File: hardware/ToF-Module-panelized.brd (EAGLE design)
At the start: 96.2 x 95.6 mm, 400 parts, among them CON1 JST-03, CON10 JST-03, CON11 JST-03, CON12 JST-03, CON13 JST-03, CON14 JST-03, CON15 JST-03, CON16 JST-03, CON17 JST-03, CON18 JST-03, CON19 JST-03, CON2 JST-03, CON20 JST-03, CON21 JST-03, CON22 JST-03, CON23 JST-03, CON24 JST-03, CON25 JST-03, CON26 JST-03, CON27 JST-03, CON28 JST-03, CON29 JST-03, CON3 JST-03, CON30 JST-03, CON31 JST-03, CON32 JST-03, CON33 JST-03, CON34 JST-03, CON35 JST-03, CON36 JST-03, CON37 JST-03, CON38 JST-03, CON39 JST-03, CON4 JST-03, CON40 JST-03, CON5 JST-03, CON6 JST-03, CON7 JST-03, CON8 JST-03, CON9 JST-03, U1 ATMEGA328P, U10 ATMEGA328P, U11 BSS138DWQ, U12 MIC5504_2.8YM5, U13 ATMEGA328P, U14 BSS138DWQ, U15 MIC5504_2.8YM5, U16 ATMEGA328P, U17 BSS138DWQ, U18 MIC5504_2.8YM5, U19 ATMEGA328P, U2 BSS138DWQ, U20 BSS138DWQ, U21 MIC5504_2.8YM5, U22 ATMEGA328P, U23 BSS138DWQ, U24 MIC5504_2.8YM5, U25 ATMEGA328P, U26 BSS138DWQ, U27 MIC5504_2.8YM5, U28 ATMEGA328P, U29 BSS138DWQ, U3 MIC5504_2.8YM5, U30 MIC5504_2.8YM5, U31 ATMEGA328P, U32 BSS138DWQ, U33 MIC5504_2.8YM5, U34 ATMEGA328P, U35 BSS138DWQ, U36 MIC5504_2.8YM5, U37 ATMEGA328P, U38 BSS138DWQ, U39 MIC5504_2.8YM5, U4 ATMEGA328P, U40 ATMEGA328P, U41 BSS138DWQ, U42 MIC5504_2.8YM5, U43 ATMEGA328P, U44 BSS138DWQ, U45 MIC5504_2.8YM5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

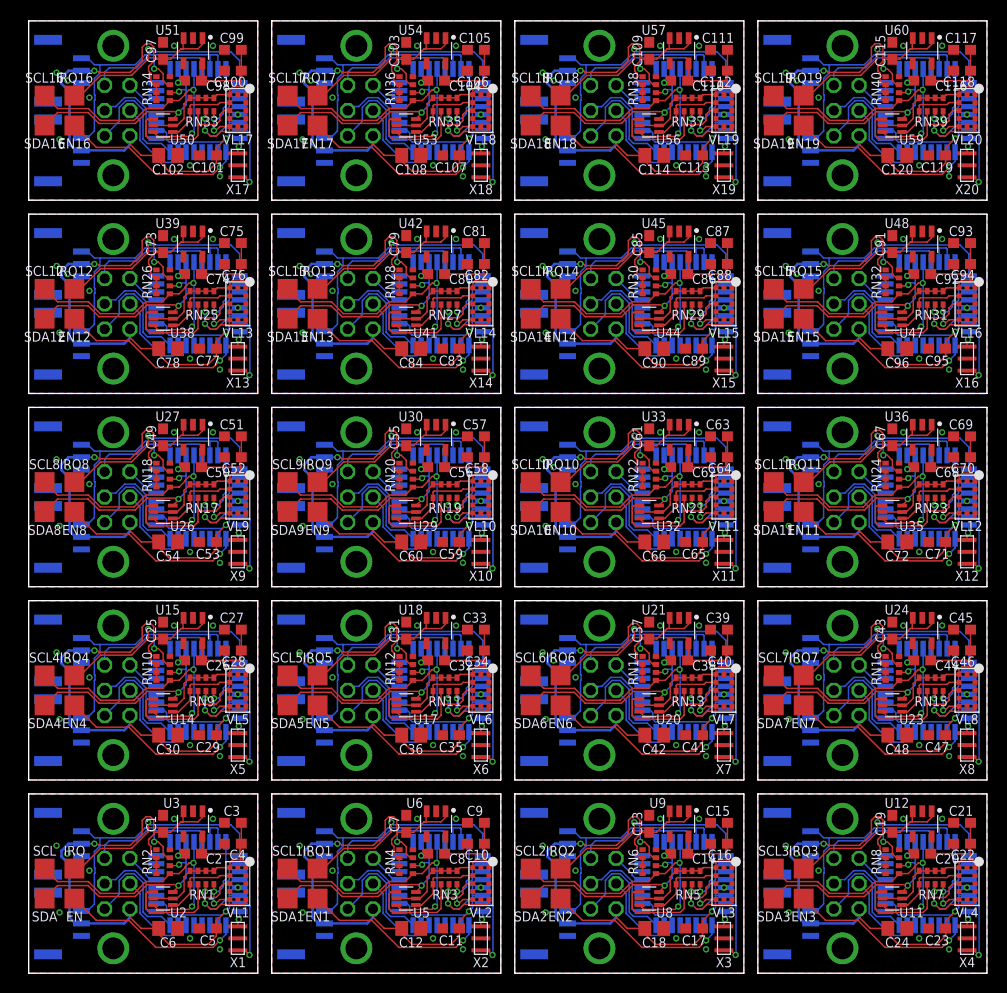
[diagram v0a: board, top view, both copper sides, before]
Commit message: hardware: add pullup for ext IRQ line + debug pads
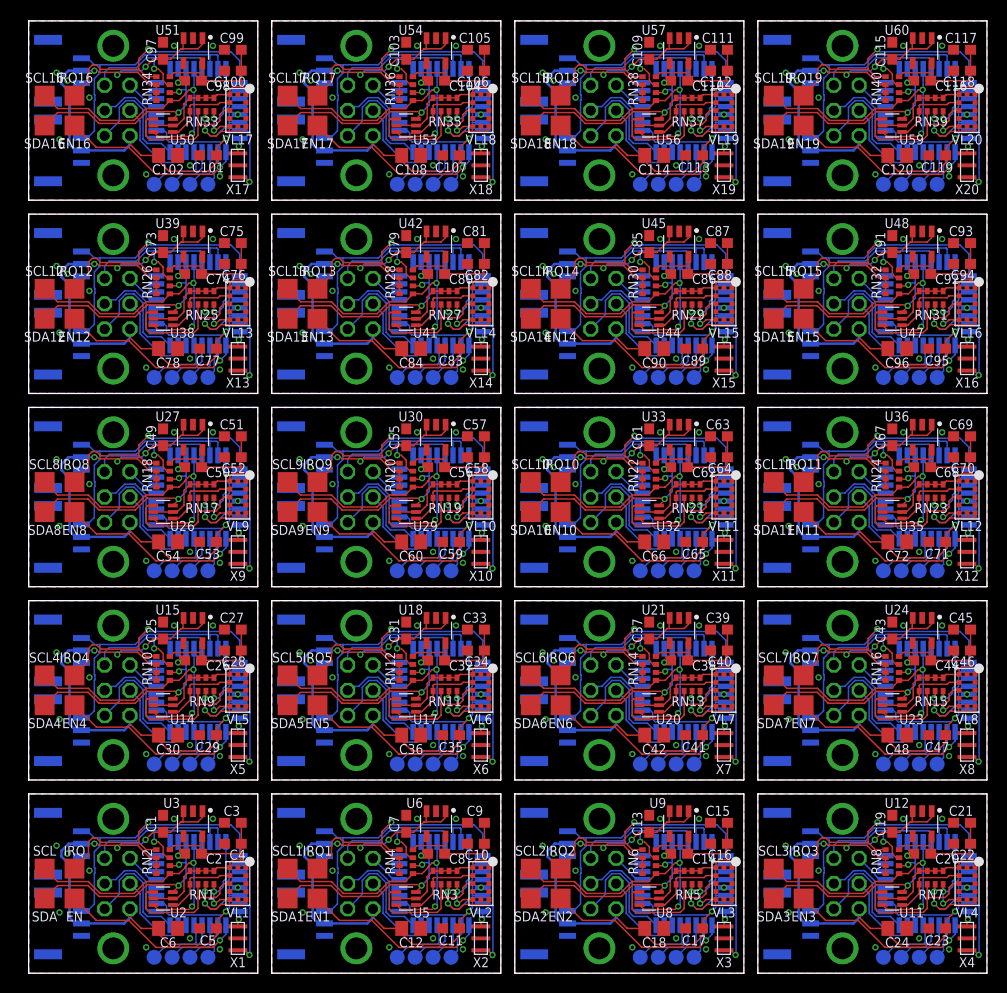
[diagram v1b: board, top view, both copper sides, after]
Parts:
- added DEBUG_A, DEBUG_A1, DEBUG_A10, DEBUG_A11, DEBUG_A12, DEBUG_A13, DEBUG_A14, DEBUG_A15, DEBUG_A16, DEBUG_A17, DEBUG_A18, DEBUG_A19, DEBUG_A2, DEBUG_A3, DEBUG_A4, DEBUG_A5, DEBUG_A6, DEBUG_A7, DEBUG_A8, DEBUG_A9, DEBUG_B, DEBUG_B1, DEBUG_B10, DEBUG_B11, DEBUG_B12, DEBUG_B13, DEBUG_B14, DEBUG_B15, DEBUG_B16, DEBUG_B17, DEBUG_B18, DEBUG_B19, DEBUG_B2, DEBUG_B3, DEBUG_B4, DEBUG_B5, DEBUG_B6, DEBUG_B7, DEBUG_B8, DEBUG_B9, DEBUG_C, DEBUG_C1, DEBUG_C10, DEBUG_C11, DEBUG_C12, DEBUG_C13, DEBUG_C14, DEBUG_C15, DEBUG_C16, DEBUG_C17, DEBUG_C18, DEBUG_C19, DEBUG_C2, DEBUG_C3, DEBUG_C4, DEBUG_C5, DEBUG_C6, DEBUG_C7, DEBUG_C8, DEBUG_C9, DEBUG_D, DEBUG_D1, DEBUG_D10, DEBUG_D11, DEBUG_D12, DEBUG_D13, DEBUG_D14, DEBUG_D15, DEBUG_D16, DEBUG_D17, DEBUG_D18, DEBUG_D19, DEBUG_D2, DEBUG_D3, DEBUG_D4, DEBUG_D5, DEBUG_D6, DEBUG_D7, DEBUG_D8, DEBUG_D9: PTR1TP15R, testpad:TP15R
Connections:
- new net N$1: DEBUG_A.TP, U1.10
- new net N$101: DEBUG_A12.TP, U37.10
- new net N$102: DEBUG_B12.TP, U37.11
- new net N$103: DEBUG_C12.TP, U37.12
- new net N$104: DEBUG_D12.TP, U37.13
- new net N$109: DEBUG_A13.TP, U40.10
- new net N$110: DEBUG_B13.TP, U40.11
- new net N$111: DEBUG_C13.TP, U40.12
- new net N$112: DEBUG_D13.TP, U40.13
- new net N$117: DEBUG_A14.TP, U43.10
- new net N$118: DEBUG_B14.TP, U43.11
- new net N$119: DEBUG_C14.TP, U43.12
- new net N$120: DEBUG_D14.TP, U43.13
- new net N$125: DEBUG_A15.TP, U46.10
- new net N$126: DEBUG_B15.TP, U46.11
- new net N$127: DEBUG_C15.TP, U46.12
- new net N$128: DEBUG_D15.TP, U46.13
- new net N$13: DEBUG_A1.TP, U4.10
- new net N$133: DEBUG_A16.TP, U49.10
- new net N$134: DEBUG_B16.TP, U49.11
- new net N$135: DEBUG_C16.TP, U49.12
- new net N$136: DEBUG_D16.TP, U49.13
- new net N$14: DEBUG_B1.TP, U4.11
- new net N$141: DEBUG_A17.TP, U52.10
- new net N$142: DEBUG_B17.TP, U52.11
- new net N$143: DEBUG_C17.TP, U52.12
- new net N$144: DEBUG_D17.TP, U52.13
- new net N$149: DEBUG_A18.TP, U55.10
- new net N$15: DEBUG_C1.TP, U4.12
- new net N$150: DEBUG_B18.TP, U55.11
- new net N$151: DEBUG_C18.TP, U55.12
- new net N$152: DEBUG_D18.TP, U55.13
- new net N$157: DEBUG_A19.TP, U58.10
- new net N$158: DEBUG_B19.TP, U58.11
- new net N$159: DEBUG_C19.TP, U58.12
- new net N$16: DEBUG_D1.TP, U4.13
- new net N$160: DEBUG_D19.TP, U58.13
- new net N$2: DEBUG_B.TP, U1.11
- new net N$21: DEBUG_A2.TP, U7.10
- new net N$22: DEBUG_B2.TP, U7.11
- new net N$23: DEBUG_C2.TP, U7.12
- new net N$24: DEBUG_D2.TP, U7.13
- new net N$29: DEBUG_A3.TP, U10.10
- new net N$30: DEBUG_B3.TP, U10.11
- new net N$31: DEBUG_C3.TP, U10.12
- new net N$32: DEBUG_D3.TP, U10.13
- new net N$37: DEBUG_A4.TP, U13.10
- new net N$38: DEBUG_B4.TP, U13.11
- new net N$39: DEBUG_C4.TP, U13.12
- new net N$40: DEBUG_D4.TP, U13.13
- new net N$45: DEBUG_A5.TP, U16.10
- new net N$46: DEBUG_B5.TP, U16.11
- new net N$47: DEBUG_C5.TP, U16.12
- new net N$48: DEBUG_D5.TP, U16.13
- new net N$53: DEBUG_A6.TP, U19.10
- new net N$54: DEBUG_B6.TP, U19.11
- new net N$55: DEBUG_C6.TP, U19.12
- new net N$56: DEBUG_D6.TP, U19.13
- new net N$61: DEBUG_A7.TP, U22.10
- new net N$62: DEBUG_B7.TP, U22.11
- new net N$63: DEBUG_C7.TP, U22.12
- new net N$64: DEBUG_D7.TP, U22.13
- new net N$69: DEBUG_A8.TP, U25.10
- new net N$7: DEBUG_C.TP, U1.12
- new net N$70: DEBUG_B8.TP, U25.11
- new net N$71: DEBUG_C8.TP, U25.12
- new net N$72: DEBUG_D8.TP, U25.13
- new net N$77: DEBUG_A9.TP, U28.10
- new net N$78: DEBUG_B9.TP, U28.11
- new net N$79: DEBUG_C9.TP, U28.12
- new net N$8: DEBUG_D.TP, U1.13
- new net N$80: DEBUG_D9.TP, U28.13
- new net N$85: DEBUG_A10.TP, U31.10
- new net N$86: DEBUG_B10.TP, U31.11
- new net N$87: DEBUG_C10.TP, U31.12
- new net N$88: DEBUG_D10.TP, U31.13
- new net N$93: DEBUG_A11.TP, U34.10
- new net N$94: DEBUG_B11.TP, U34.11
- new net N$95: DEBUG_C11.TP, U34.12
- new net N$96: DEBUG_D11.TP, U34.13
- net +2V1: now also RN4.4
- net +2V10: now also RN20.4
- net +2V11: now also RN22.4
- net +2V12: now also RN24.4
- net +2V13: now also RN26.4
- net +2V14: now also RN28.4
- net +2V15: now also RN30.4
- net +2V16: now also RN32.4
- net +2V17: now also RN34.4
- net +2V18: now also RN36.4
- net +2V19: now also RN38.4
- net +2V2: now also RN6.4
- net +2V20: now also RN40.4
- net +2V3: now also RN8.4
- net +2V4: now also RN10.4
- net +2V5: now also RN12.4
- net +2V6: now also RN14.4
- net +2V7: now also RN16.4
- net +2V8: now also RN2.4
- net +2V9: now also RN18.4
- net EXT_IRQ: now also RN2.5
- net EXT_IRQ1: now also RN4.5
- net EXT_IRQ10: now also RN22.5
- net EXT_IRQ11: now also RN24.5
- net EXT_IRQ12: now also RN26.5
- net EXT_IRQ13: now also RN28.5
- net EXT_IRQ14: now also RN30.5
- net EXT_IRQ15: now also RN32.5
- net EXT_IRQ16: now also RN34.5
- net EXT_IRQ17: now also RN36.5
- net EXT_IRQ18: now also RN38.5
- net EXT_IRQ19: now also RN40.5
- net EXT_IRQ2: now also RN6.5
- net EXT_IRQ3: now also RN8.5
- net EXT_IRQ4: now also RN10.5
- net EXT_IRQ5: now also RN12.5
- net EXT_IRQ6: now also RN14.5
- net EXT_IRQ7: now also RN16.5
- net EXT_IRQ8: now also RN18.5
- net EXT_IRQ9: now also RN20.5
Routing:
- net N$64: track 0.00 -> 6.65 mm
- net N$160: track 0.00 -> 6.65 mm
- net N$32: track 0.00 -> 6.65 mm
- net N$96: track 0.00 -> 6.65 mm
- net N$128: track 0.00 -> 6.65 mm
- net N$40: track 0.00 -> 6.65 mm
- net N$8: track 0.00 -> 6.65 mm
- net N$136: track 0.00 -> 6.65 mm
- net N$56: track 0.00 -> 6.65 mm
- net N$72: track 0.00 -> 6.65 mm
- net N$152: track 0.00 -> 6.65 mm
- net N$104: track 0.00 -> 6.65 mm
- net N$24: track 0.00 -> 6.65 mm
- net N$88: track 0.00 -> 6.65 mm
- net N$120: track 0.00 -> 6.65 mm
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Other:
- board text added: "A"
- board text added: "B"
- board text added: "C"
- board text added: "D"
